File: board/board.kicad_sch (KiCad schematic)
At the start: 63 parts, among them J3 Conn_01x25_Socket, J4 Conn_01x25_Socket, J5 PJ-320B, J6 Screw_Terminal_01x02, J7 Screw_Terminal_01x02, J8 Screw_Terminal_01x02

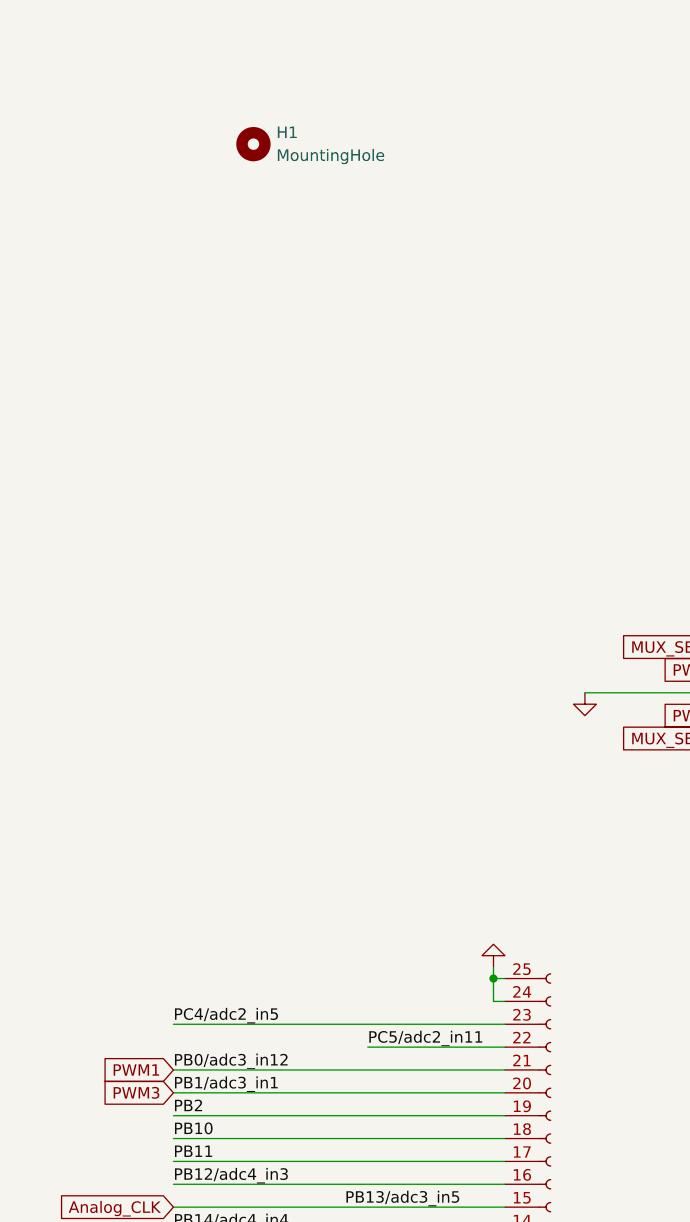
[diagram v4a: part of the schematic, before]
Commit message: added separate connector for UART
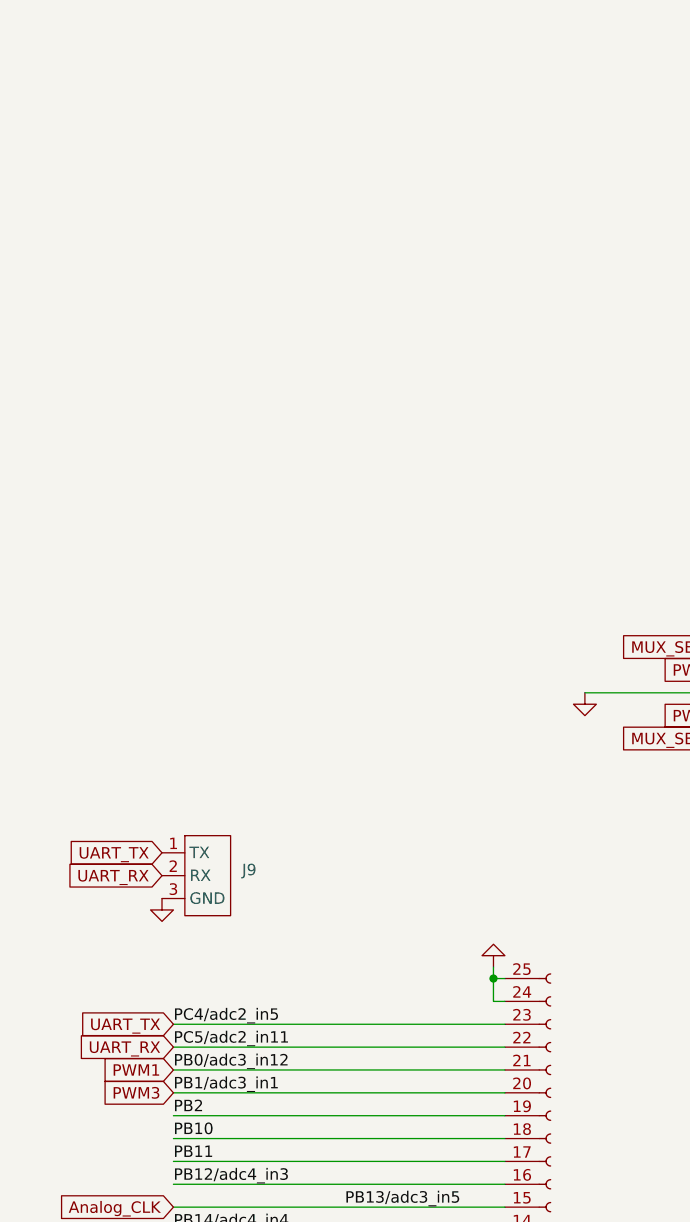
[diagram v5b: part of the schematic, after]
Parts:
- removed H1: MountingHole, MountingHole:MountingHole_3.2mm_M3, symbol Mechanical:MountingHole
- added J9: ~, project:UART_port, symbol project:UART_port
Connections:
- net GND: now also J9.3 (GND)
- net PC4/adc2_in5 renamed UART_TX
- net UART_TX: now also J9.1 (TX)
- net PC5/adc2_in11 renamed UART_RX
- net UART_RX: now also J9.2 (RX)
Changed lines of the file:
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@@
 	(wire
 		(pts
-			(xy 85.09 127) (xy 69.85 127)
+			(xy 48.26 127) (xy 85.09 127)
 		)
 		(stroke
@@
 	)
 	(label "PC5{slash}adc2_in11"
-		(at 69.85 127 0)
+		(at 48.26 127 0)
 		(fields_autoplaced yes)
 		(effects
@@
 		)
 	)
+	(global_label "UART_TX"
+		(shape input)
+		(at 46.99 105.41 180)
+		(fields_autoplaced yes)
+		(effects
+			(font
+				(size 1.27 1.27)
+			)
+			(justify right)
+		)
+		(property "Intersheetrefs" "${INTERSHEET_REFS}"
+			(at 36.2034 105.41 0)
+			(effects
+				(font
+					(size 1.27 1.27)
+				)
+				(justify right)
+				(hide yes)
+			)
+		)
+	)
 	(global_label "FLASH_MOSI"
 		(shape input)
@@
 		)
 	)
+	(global_label "UART_RX"
+		(shape input)
+		(at 48.26 127 180)
+		(fields_autoplaced yes)
+		(effects
+			(font
+				(size 1.27 1.27)
+			)
+			(justify right)
+		)
+		(property "Intersheetrefs" "${INTERSHEET_REFS}"
+			(at 37.171 127 0)
+			(effects
+				(font
+					(size 1.27 1.27)
+				)
+				(justify right)
+				(hide yes)
+			)
+		)
+	)
 	(global_label "CH2_OUT"
 		(shape input)
@@
 		)
 	)
+	(global_label "UART_RX"
+		(shape input)
+		(at 46.99 107.95 180)
+		(fields_autoplaced yes)
+		(effects
+			(font
+				(size 1.27 1.27)
+			)
+			(justify right)
+		)
+		(property "Intersheetrefs" "${INTERSHEET_REFS}"
+			(at 35.901 107.95 0)
+			(effects
+				(font
+					(size 1.27 1.27)
+				)
+				(justify right)
+				(hide yes)
+			)
+		)
+	)
 	(global_label "CH4_TOFILT"
 		(shape input)
@@
 		)
 	)
+	(global_label "UART_TX"
+		(shape input)
+		(at 48.26 124.46 180)
+		(fields_autoplaced yes)
+		(effects
+			(font
+				(size 1.27 1.27)
+			)
+			(justify right)
+		)
+		(property "Intersheetrefs" "${INTERSHEET_REFS}"
+			(at 37.4734 124.46 0)
+			(effects
+				(font
+					(size 1.27 1.27)
+				)
+				(justify right)
+				(hide yes)
+			)
+		)
+	)
 	(global_label "Analog_CLK"
 		(shape input)
@@
 	)
 	(symbol
+		(lib_id "power:GND")
+		(at 46.99 110.49 0)
+		(unit 1)
+		(exclude_from_sim no)
+		(in_bom yes)
+		(on_board yes)
+		(dnp no)
+		(fields_autoplaced yes)
+		(property "Reference" "#PWR089"
+			(at 46.99 116.84 0)
+			(effects
+				(font
+					(size 1.27 1.27)
+				)
+				(hide yes)
+			)
+		)
+		(property "Value" "GND"
+			(at 46.99 115.57 0)
+			(effects
+				(font
+					(size 1.27 1.27)
+				)
+				(hide yes)
+			)
+		)
+		(property "Footprint" ""
+			(at 46.99 110.49 0)
+			(effects
+				(font
+					(size 1.27 1.27)
+				)
+				(hide yes)
+			)
+		)
+		(property "Datasheet" ""
+			(at 46.99 110.49 0)
+			(effects
+				(font
+					(size 1.27 1.27)
+				)
+				(hide yes)
+			)
+		)
+		(property "Description" "Power symbol creates a global label with name \"GND\" , ground"
+			(at 46.99 110.49 0)
+			(effects
+				(font
+					(size 1.27 1.27)
+				)
+				(hide yes)
+			)
+		)
+		(pin "1"
+		)
+		(instances
+			(project "board"
+				(path "/e8cec806-e837-4d6f-b166-2de75a563bd6"
+					(reference "#PWR089")
+					(unit 1)
+				)
+			)
+		)
+	)
+	(symbol
 		(lib_id "Generic:P,-15")
 		(at 181.61 170.18 0)
@@
 	)
 	(symbol
-		(lib_id "power:GND")
-		(at 194.1628 228.6 0)
+		(lib_id "project:UART_port")
+		(at 52.07 105.41 0)
 		(unit 1)
 		(exclude_from_sim no)
@@
 		(dnp no)
 		(fields_autoplaced yes)
-		(property "Reference" "#PWR063"
-			(at 194.1628 234.95 0)
+		(property "Reference" "J9"
+			(at 55.88 107.3149 0)
 			(effects
 				(font
 					(size 1.27 1.27)
 				)
-				(hide yes)
+				(justify left)
 			)
 		)
-		(property "Value" "GND"
-			(at 194.1628 233.68 0)
+		(property "Value" "~"
+			(at 55.88 109.22 0)
 			(effects
 				(font
 					(size 1.27 1.27)
 				)
-				(hide yes)
+				(justify left)
 			)
 		)
-		(property "Footprint" ""
-			(at 194.1628 228.6 0)
+		(property "Footprint" "project:UART_port"
+			(at 46.99 105.41 0)
 			(effects
 				(font
@@
 		)
 		(property "Datasheet" ""
-			(at 194.1628 228.6 0)
+			(at 46.99 105.41 0)
 			(effects
 				(font
@@
 			)
 		)
-		(property "Description" "Power symbol creates a global label with name \"GND\" , ground"
-			(at 194.1628 228.6 0)
+		(property "Description" ""
+			(at 46.99 105.41 0)
 			(effects
 				(font
@@
 		(pin "1"
 		)
+		(pin "2"
+		)
+		(pin "3"
+		)
 		(instances
 			(project "board"
 				(path "/e8cec806-e837-4d6f-b166-2de75a563bd6"
-					(reference "#PWR063")
+					(reference "J9")
 					(unit 1)
 				)
@@
 	)
 	(symbol
-		(lib_id "Mechanical:MountingHole")
-		(at 57.15 26.67 0)
+		(lib_id "power:GND")
+		(at 194.1628 228.6 0)
 		(unit 1)
-		(exclude_from_sim yes)
-		(in_bom no)
+		(exclude_from_sim no)
+		(in_bom yes)
 		(on_board yes)
 		(dnp no)
 		(fields_autoplaced yes)
-		(property "Reference" "H1"
-			(at 59.69 25.3999 0)
+		(property "Reference" "#PWR063"
+			(at 194.1628 234.95 0)
 			(effects
 				(font
 					(size 1.27 1.27)
 				)
-				(justify left)
+				(hide yes)
 			)
 		)
-		(property "Value" "MountingHole"
-			(at 59.69 27.9399 0)
+		(property "Value" "GND"
+			(at 194.1628 233.68 0)
 			(effects
 				(font
 					(size 1.27 1.27)
 				)
-				(justify left)
+				(hide yes)
 			)
 		)
-		(property "Footprint" "MountingHole:MountingHole_3.2mm_M3"
-			(at 57.15 26.67 0)
+		(property "Footprint" ""
+			(at 194.1628 228.6 0)
 			(effects
 				(font
@@
 			)
 		)
-		(property "Datasheet" "~"
-			(at 57.15 26.67 0)
+		(property "Datasheet" ""
+			(at 194.1628 228.6 0)
 			(effects
 				(font
@@
 			)
 		)
-		(property "Description" "Mounting Hole without connection"
-			(at 57.15 26.67 0)
+		(property "Description" "Power symbol creates a global label with name \"GND\" , ground"
+			(at 194.1628 228.6 0)
 			(effects
 				(font
@@
 			)
 		)
+		(pin "1"
+		)
 		(instances
 			(project "board"
 				(path "/e8cec806-e837-4d6f-b166-2de75a563bd6"
-					(reference "H1")
+					(reference "#PWR063")
 					(unit 1)
 				)
